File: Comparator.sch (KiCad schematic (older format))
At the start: 0 parts

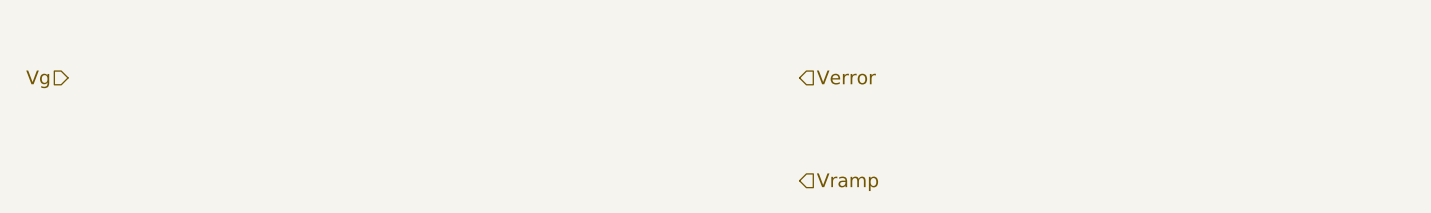
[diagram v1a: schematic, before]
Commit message: Finished the full circuit.
All thats left is to set the design parameters.
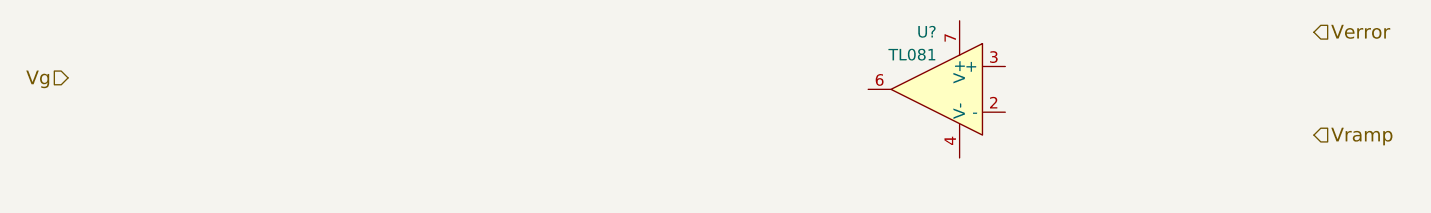
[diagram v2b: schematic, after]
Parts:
- added U?: TL081, symbol TL081
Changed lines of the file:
@@
 Text HLabel 2500 2500 0    60   Input ~ 0
 Vg
-Text HLabel 5700 2500 2    60   Input ~ 0
+Text HLabel 7950 2300 2    60   Input ~ 0
 Verror
-Text HLabel 5700 2950 2    60   Input ~ 0
+Text HLabel 7950 2750 2    60   Input ~ 0
 Vramp
+$Comp
+L TL081 U?
+U 1 1 58B85DF2
+P 6300 2550
+F 0 "U?" H 6300 2800 50  0000 L CNN
+F 1 "TL081" H 6300 2700 50  0000 L CNN
+F 2 "" H 6350 2750 50  0000 C CNN
+F 3 "" H 6300 2800 50  0000 C CNN
+	1    6300 2550
+	-1   0    0    -1
+$EndComp
 $EndSCHEMATC
